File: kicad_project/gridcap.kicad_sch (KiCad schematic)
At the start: 69 parts, among them J1 Conn_01x10

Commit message: Add all pads to pcb
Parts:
- PAD17, PAD18, PAD19, PAD20, PAD21, PAD22, PAD23, PAD24, PAD25, PAD26, PAD27, PAD28, PAD29, PAD30, PAD31, PAD32, PAD33, PAD34, PAD35, PAD36, PAD37, PAD38, PAD39, PAD40, PAD41, PAD42, PAD43, PAD44, PAD45, PAD46, PAD47, PAD48, PAD49, PAD50, PAD51, PAD52, PAD53, PAD54, PAD55, PAD56, PAD57, PAD58, PAD59, PAD60, PAD61, PAD62, PAD63, PAD64: footprint (none) -> gridcap_footprints:CAPACITOR_PAD

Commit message: Fix pad pin number
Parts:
- MUX1, MUX2, MUX3, MUX4, PAD1, PAD10, PAD11, PAD12, PAD13, PAD14, PAD15, PAD16, PAD17, PAD18, PAD19, PAD2, PAD20, PAD21, PAD22, PAD23, PAD24, PAD25, PAD26, PAD27, PAD28, PAD29, PAD3, PAD30, PAD31, PAD32, PAD33, PAD34, PAD35, PAD36, PAD37, PAD38, PAD39, PAD4, PAD40, PAD41, PAD42, PAD43, PAD44, PAD45, PAD46, PAD47, PAD48, PAD49, PAD5, PAD50, PAD51, PAD52, PAD53, PAD54, PAD55, PAD56, PAD57, PAD58, PAD59, PAD6, PAD60, PAD61, PAD62, PAD63, PAD64, PAD7, PAD8, PAD9: value ~ -> (none)
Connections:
- net at MUX2.6 (Y3): now also PAD25.1; no longer PAD25.
- net at MUX2.20 (Y11): now also PAD24.1; no longer PAD24.
- net at MUX4.7 (Y2): now also PAD59.1; no longer PAD59.
- net at MUX3.22 (Y9): now also PAD36.1; no longer PAD36.
- net at MUX4.17 (Y14): now also PAD62.1; no longer PAD62.
- net at MUX2.9 (Y0): now also PAD31.1; no longer PAD31.
- net at MUX2.4 (Y5): now also PAD21.1; no longer PAD21.
- net at MUX1.8 (Y1): now also PAD7.1; no longer PAD7.
- net at MUX2.16 (Y15): now also PAD32.1; no longer PAD32.
- net at MUX4.5 (Y4): now also PAD55.1; no longer PAD55.
- net at MUX2.22 (Y9): now also PAD20.1; no longer PAD20.
- net at MUX3.4 (Y5): now also PAD37.1; no longer PAD37.
- net at MUX2.8 (Y1): now also PAD29.1; no longer PAD29.
- net at MUX3.5 (Y4): now also PAD39.1; no longer PAD39.
- net at MUX1.6 (Y3): now also PAD5.1; no longer PAD5.
- net at MUX1.19 (Y12): now also PAD13.1; no longer PAD13.
- net at MUX2.19 (Y12): now also PAD26.1; no longer PAD26.
- net at MUX3.3 (Y6): now also PAD35.1; no longer PAD35.
- net at MUX4.9 (Y0): now also PAD63.1; no longer PAD63.
- net at MUX3.8 (Y1): now also PAD45.1; no longer PAD45.
- net at MUX4.8 (Y1): now also PAD61.1; no longer PAD61.
- net at MUX4.23 (Y8): now also PAD50.1; no longer PAD50.
- net at MUX2.7 (Y2): now also PAD27.1; no longer PAD27.
- net at MUX2.5 (Y4): now also PAD23.1; no longer PAD23.
- net at MUX2.17 (Y14): now also PAD30.1; no longer PAD30.
- net at MUX3.7 (Y2): now also PAD43.1; no longer PAD43.
- net at MUX2.18 (Y13): now also PAD28.1; no longer PAD28.
- net at MUX2.2 (Y7): now also PAD17.1; no longer PAD17.
- net at MUX2.21 (Y10): now also PAD22.1; no longer PAD22.
- net at MUX2.23 (Y8): now also PAD18.1; no longer PAD18.
- net at MUX2.3 (Y6): now also PAD19.1; no longer PAD19.
- net at MUX1.16 (Y15): now also PAD16.1; no longer PAD16.
- net at MUX1.17 (Y14): now also PAD15.1; no longer PAD15.
- net at MUX1.18 (Y13): now also PAD14.1; no longer PAD14.
- net at MUX1.2 (Y7): now also PAD1.1; no longer PAD1.
- net at MUX1.20 (Y11): now also PAD12.1; no longer PAD12.
- net at MUX1.21 (Y10): now also PAD11.1; no longer PAD11.
- net at MUX1.22 (Y9): now also PAD10.1; no longer PAD10.
- net at MUX1.23 (Y8): now also PAD9.1; no longer PAD9.
- net at MUX1.3 (Y6): now also PAD2.1; no longer PAD2.
- net at MUX1.4 (Y5): now also PAD3.1; no longer PAD3.
- net at MUX1.5 (Y4): now also PAD4.1; no longer PAD4.
- net at MUX1.7 (Y2): now also PAD6.1; no longer PAD6.
- net at MUX1.9 (Y0): now also PAD8.1; no longer PAD8.
- net at MUX3.18 (Y13): now also PAD44.1; no longer PAD44.
- net at MUX4.16 (Y15): now also PAD64.1; no longer PAD64.
- net at MUX4.18 (Y13): now also PAD60.1; no longer PAD60.
- net at MUX4.19 (Y12): now also PAD58.1; no longer PAD58.
- net at MUX4.2 (Y7): now also PAD49.1; no longer PAD49.
- net at MUX4.20 (Y11): now also PAD56.1; no longer PAD56.
- net at MUX4.21 (Y10): now also PAD54.1; no longer PAD54.
- net at MUX4.22 (Y9): now also PAD52.1; no longer PAD52.
- net at MUX4.3 (Y6): now also PAD51.1; no longer PAD51.
- net at MUX4.4 (Y5): now also PAD53.1; no longer PAD53.
- net at MUX4.6 (Y3): now also PAD57.1; no longer PAD57.
- net at MUX3.16 (Y15): now also PAD48.1; no longer PAD48.
- net at MUX3.17 (Y14): now also PAD46.1; no longer PAD46.
- net at MUX3.19 (Y12): now also PAD42.1; no longer PAD42.
- net at MUX3.2 (Y7): now also PAD33.1; no longer PAD33.
- net at MUX3.20 (Y11): now also PAD40.1; no longer PAD40.
- net at MUX3.21 (Y10): now also PAD38.1; no longer PAD38.
- net at MUX3.23 (Y8): now also PAD34.1; no longer PAD34.
- net at MUX3.6 (Y3): now also PAD41.1; no longer PAD41.
- net at MUX3.9 (Y0): now also PAD47.1; no longer PAD47.

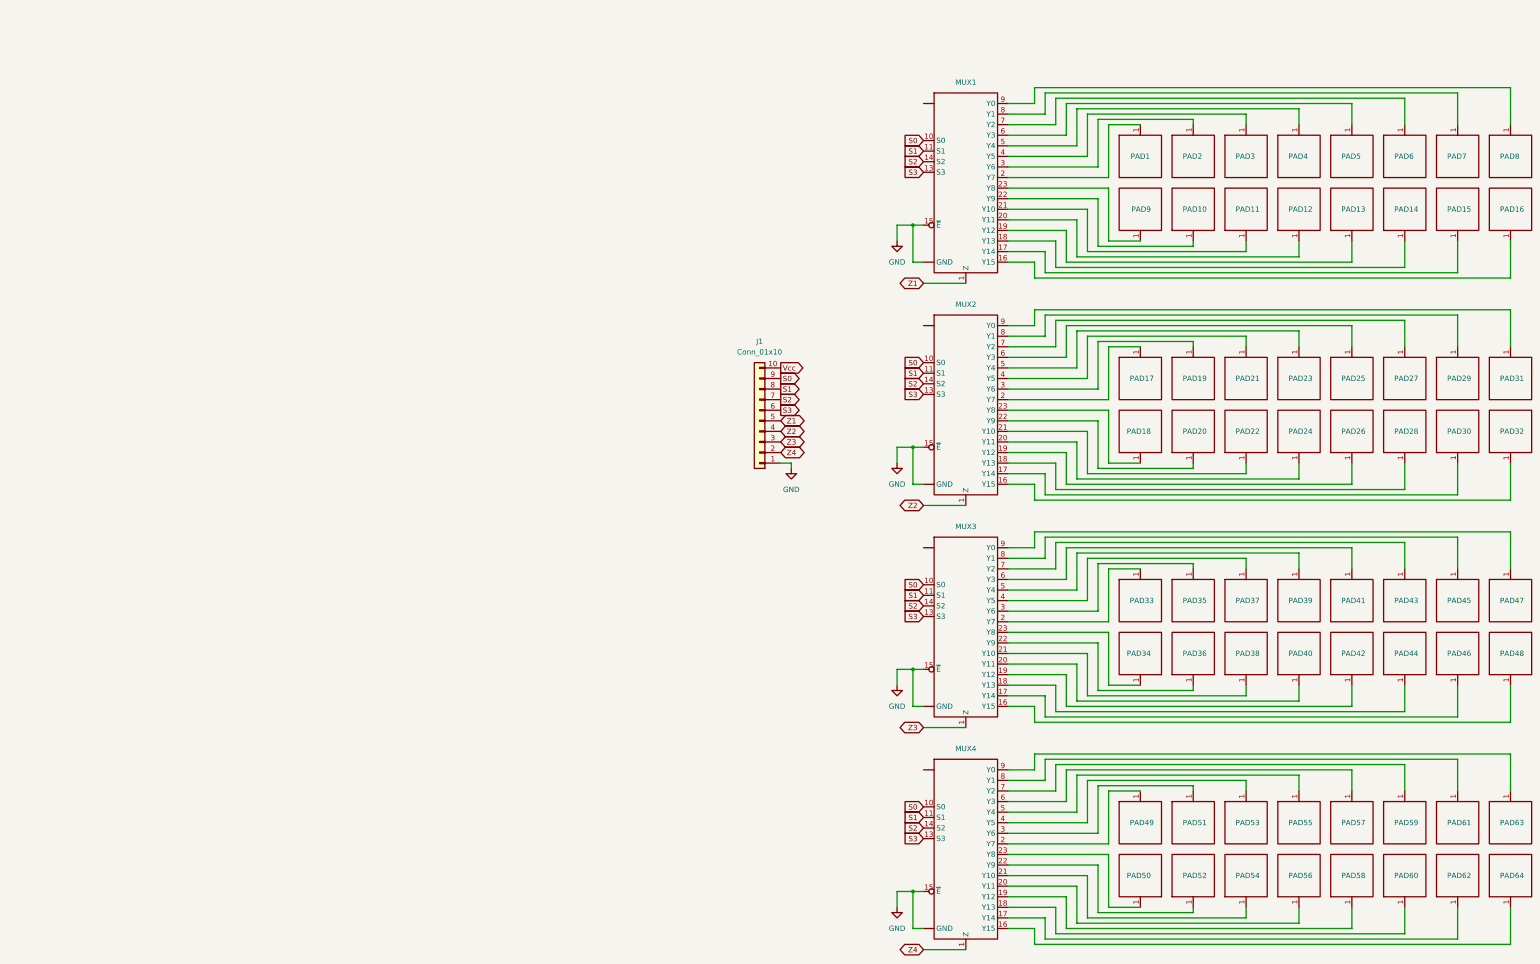
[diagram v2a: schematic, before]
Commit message: Begin rewiring pads and muxes
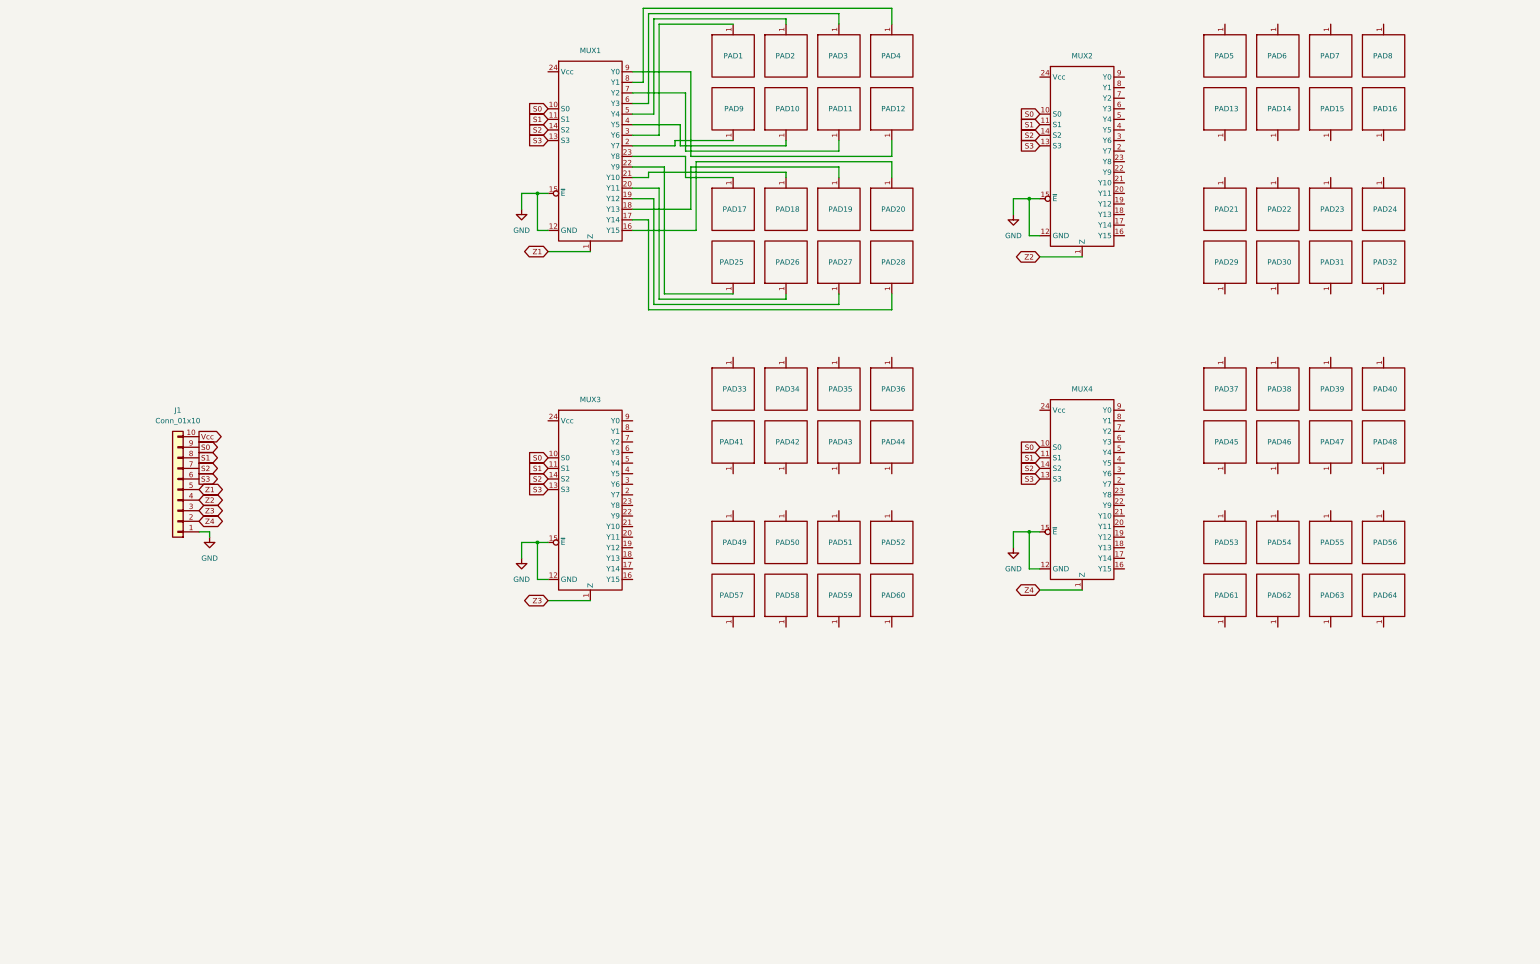
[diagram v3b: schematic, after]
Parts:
- MUX1, MUX2, MUX3, MUX4, PAD1, PAD10, PAD11, PAD12, PAD13, PAD14, PAD15, PAD16, PAD17, PAD18, PAD19, PAD2, PAD20, PAD21, PAD22, PAD23, PAD24, PAD25, PAD26, PAD27, PAD28, PAD29, PAD3, PAD30, PAD31, PAD32, PAD33, PAD34, PAD35, PAD36, PAD37, PAD38, PAD39, PAD4, PAD40, PAD41, PAD42, PAD43, PAD44, PAD45, PAD46, PAD47, PAD48, PAD49, PAD5, PAD50, PAD51, PAD52, PAD53, PAD54, PAD55, PAD56, PAD57, PAD58, PAD59, PAD6, PAD60, PAD61, PAD62, PAD63, PAD64, PAD7, PAD8, PAD9: value (none) -> ~
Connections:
- net GND: now also MUX1.12 (GND), MUX2.12 (GND), MUX3.12 (GND), MUX4.12 (GND); no longer MUX1. (GND), MUX2. (GND), MUX3. (GND), MUX4. (GND)
- net at PAD25.1: now also MUX1.22 (Y9); no longer MUX2.6 (Y3)
- net at PAD24.1: no longer MUX2.20 (Y11)
- net at PAD59.1: no longer MUX4.7 (Y2)
- net at PAD36.1: no longer MUX3.22 (Y9)
- net at PAD62.1: no longer MUX4.17 (Y14)
- net at PAD31.1: no longer MUX2.9 (Y0)
- net at PAD21.1: no longer MUX2.4 (Y5)
- net at PAD7.1: no longer MUX1.8 (Y1)
- net at PAD32.1: no longer MUX2.16 (Y15)
- net at PAD55.1: no longer MUX4.5 (Y4)
- net at PAD20.1: now also MUX1.16 (Y15); no longer MUX2.22 (Y9)
- net at PAD37.1: no longer MUX3.4 (Y5)
- net at PAD29.1: no longer MUX2.8 (Y1)
- net at PAD39.1: no longer MUX3.5 (Y4)
- net at PAD5.1: no longer MUX1.6 (Y3)
- net at PAD13.1: no longer MUX1.19 (Y12)
- net at PAD26.1: now also MUX1.20 (Y11); no longer MUX2.19 (Y12)
- net at PAD35.1: no longer MUX3.3 (Y6)
- net at PAD63.1: no longer MUX4.9 (Y0)
- net at PAD45.1: no longer MUX3.8 (Y1)
- net at PAD61.1: no longer MUX4.8 (Y1)
- net at PAD50.1: no longer MUX4.23 (Y8)
- net at PAD27.1: now also MUX1.19 (Y12); no longer MUX2.7 (Y2)
- net at PAD23.1: no longer MUX2.5 (Y4)
- net at PAD30.1: no longer MUX2.17 (Y14)
- net at PAD43.1: no longer MUX3.7 (Y2)
- net at MUX2.18 (Y13): no longer PAD28.1
- net at MUX2.2 (Y7): no longer PAD17.1
- net at MUX2.21 (Y10): no longer PAD22.1
- net at MUX2.23 (Y8): no longer PAD18.1
- net at MUX2.3 (Y6): no longer PAD19.1
- net at PAD16.1: no longer MUX1.16 (Y15)
- net at MUX1.17 (Y14): now also PAD28.1; no longer PAD15.1
- net at MUX1.18 (Y13): now also PAD19.1; no longer PAD14.1
- net at MUX1.2 (Y7): now also PAD9.1; no longer PAD1.1
- net at PAD12.1: now also MUX1.9 (Y0); no longer MUX1.20 (Y11)
- net at MUX1.21 (Y10): now also PAD18.1; no longer PAD11.1
- net at PAD10.1: now also MUX1.4 (Y5); no longer MUX1.22 (Y9)
- net at MUX1.23 (Y8): now also PAD17.1; no longer PAD9.1
- net at MUX1.3 (Y6): now also PAD1.1; no longer PAD2.1
- net at PAD3.1: now also MUX1.6 (Y3); no longer MUX1.4 (Y5)
- net at MUX1.5 (Y4): now also PAD2.1; no longer PAD4.1
- net at MUX1.7 (Y2): now also PAD11.1; no longer PAD6.1
- net at PAD8.1: no longer MUX1.9 (Y0)
- net at PAD44.1: no longer MUX3.18 (Y13)
- net at MUX4.16 (Y15): no longer PAD64.1
- net at MUX4.18 (Y13): no longer PAD60.1
- net at MUX4.19 (Y12): no longer PAD58.1
- net at MUX4.2 (Y7): no longer PAD49.1
- net at MUX4.20 (Y11): no longer PAD56.1
- net at MUX4.21 (Y10): no longer PAD54.1
- net at MUX4.22 (Y9): no longer PAD52.1
- net at MUX4.3 (Y6): no longer PAD51.1
- net at MUX4.4 (Y5): no longer PAD53.1
- net at MUX4.6 (Y3): no longer PAD57.1
- net at MUX3.16 (Y15): no longer PAD48.1
- net at MUX3.17 (Y14): no longer PAD46.1
- net at MUX3.19 (Y12): no longer PAD42.1
- net at MUX3.2 (Y7): no longer PAD33.1
- net at MUX3.20 (Y11): no longer PAD40.1
- net at MUX3.21 (Y10): no longer PAD38.1
- net at MUX3.23 (Y8): no longer PAD34.1
- net at MUX3.6 (Y3): no longer PAD41.1
- net at MUX3.9 (Y0): no longer PAD47.1
- new net: MUX1.8 (Y1), PAD4.1
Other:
- moved on the sheet: J1, PAD1, PAD10, PAD11, PAD12, PAD13, PAD14, PAD15, PAD16, PAD17, PAD18, PAD19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

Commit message: Route all muxes to pads
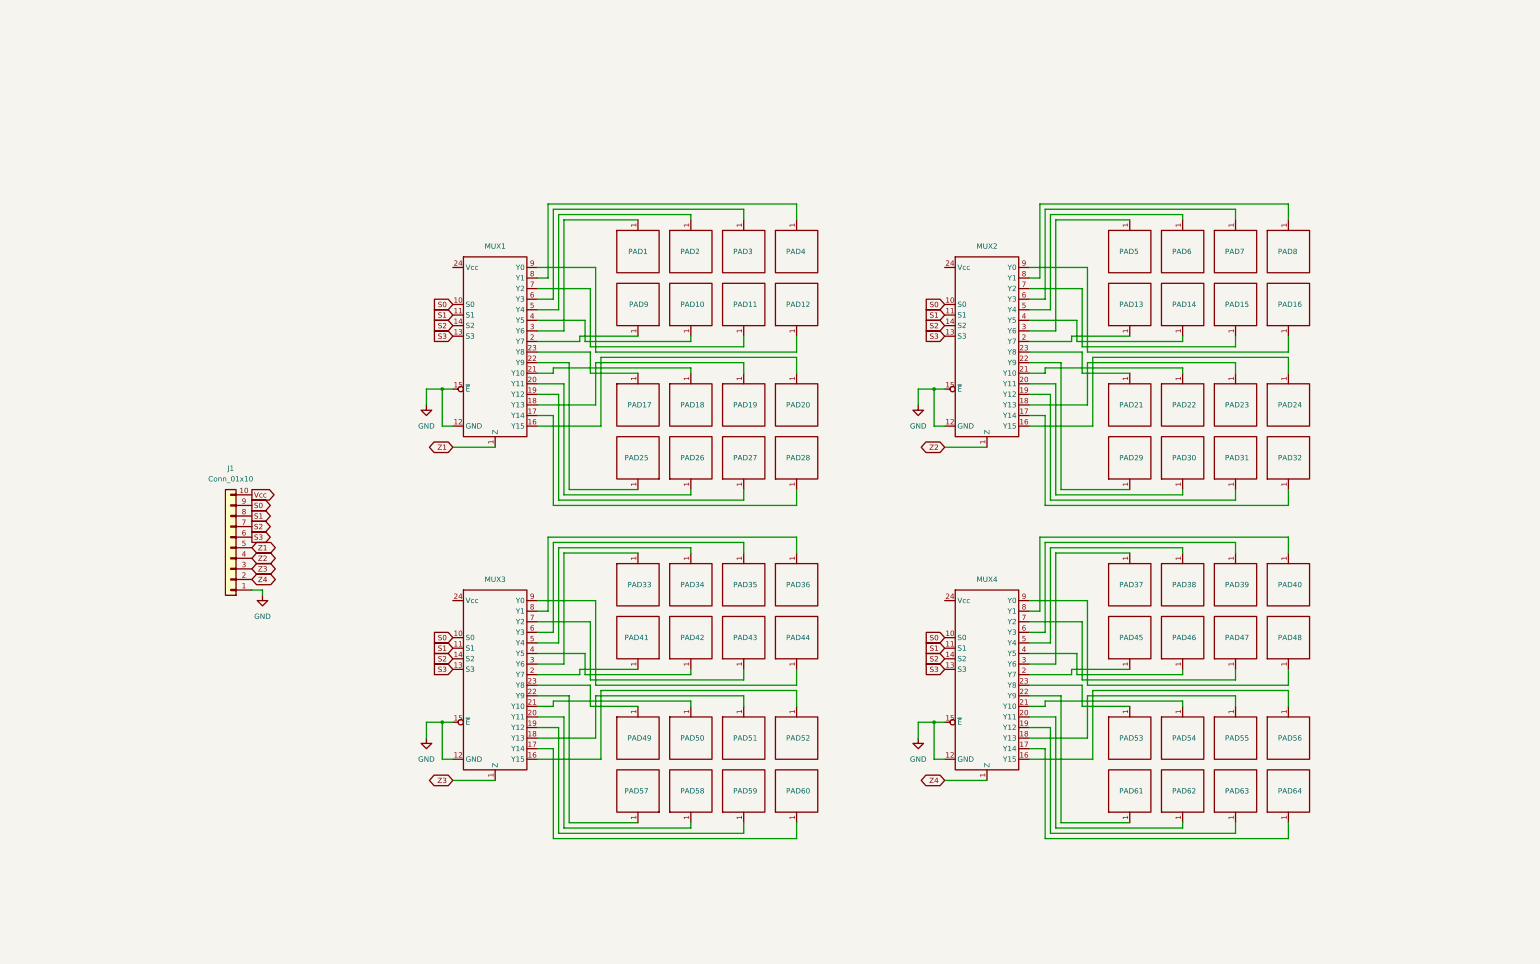
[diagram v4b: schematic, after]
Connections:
- net at PAD24.1: now also MUX2.16 (Y15)
- net at PAD59.1: now also MUX3.19 (Y12)
- net at PAD36.1: now also MUX3.8 (Y1)
- net at PAD62.1: now also MUX4.20 (Y11)
- net at PAD31.1: now also MUX2.19 (Y12)
- net at PAD21.1: now also MUX2.23 (Y8)
- net at PAD7.1: now also MUX2.6 (Y3)
- net at PAD32.1: now also MUX2.17 (Y14)
- net at PAD55.1: now also MUX4.18 (Y13)
- net at PAD37.1: now also MUX4.3 (Y6)
- net at PAD29.1: now also MUX2.22 (Y9)
- net at PAD39.1: now also MUX4.6 (Y3)
- net at PAD5.1: now also MUX2.3 (Y6)
- net at PAD13.1: now also MUX2.2 (Y7)
- net at PAD35.1: now also MUX3.6 (Y3)
- net at PAD63.1: now also MUX4.19 (Y12)
- net at PAD45.1: now also MUX4.2 (Y7)
- net at PAD61.1: now also MUX4.22 (Y9)
- net at PAD50.1: now also MUX3.21 (Y10)
- net at PAD23.1: now also MUX2.18 (Y13)
- net at PAD30.1: now also MUX2.20 (Y11)
- net at PAD43.1: now also MUX3.7 (Y2)
- net at MUX2.21 (Y10): now also PAD22.1
- net at MUX2.4 (Y5): now also PAD14.1
- net at MUX2.5 (Y4): now also PAD6.1
- net at MUX2.7 (Y2): now also PAD15.1
- net at MUX2.8 (Y1): now also PAD8.1
- net at MUX2.9 (Y0): now also PAD16.1
- net at PAD44.1: now also MUX3.9 (Y0)
- net at MUX4.16 (Y15): now also PAD56.1
- net at MUX4.17 (Y14): now also PAD64.1
- net at MUX4.21 (Y10): now also PAD54.1
- net at MUX4.23 (Y8): now also PAD53.1
- net at MUX4.4 (Y5): now also PAD46.1
- net at MUX4.5 (Y4): now also PAD38.1
- net at MUX4.7 (Y2): now also PAD47.1
- net at MUX4.8 (Y1): now also PAD40.1
- net at MUX4.9 (Y0): now also PAD48.1
- net at PAD60.1: now also MUX3.17 (Y14)
- net at MUX3.16 (Y15): now also PAD52.1
- net at MUX3.18 (Y13): now also PAD51.1
- net at MUX3.2 (Y7): now also PAD41.1
- net at MUX3.20 (Y11): now also PAD58.1
- net at MUX3.22 (Y9): now also PAD57.1
- net at MUX3.23 (Y8): now also PAD49.1
- net at MUX3.3 (Y6): now also PAD33.1
- net at MUX3.4 (Y5): now also PAD42.1
- net at MUX3.5 (Y4): now also PAD34.1
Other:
- moved on the sheet: J1, MUX1, MUX2, MUX3, MUX4, PAD1, PAD10, PAD11, PAD12, PAD13, PAD14, PAD15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

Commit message: Route all muxes and add pcb shape
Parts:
- J1: footprint (none) -> Connector_PinHeader_2.54mm:PinHeader_1x10_P2.54mm_Vertical
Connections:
- net Vcc: now also MUX1.24 (Vcc), MUX2.24 (Vcc), MUX3.24 (Vcc), MUX4.24 (Vcc)
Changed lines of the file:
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@@
+    )
+  )
+  (global_label "Vcc" (shape input) (at 129.54 81.28 180) (fields_autoplaced)
+    (effects (font (size 1.27 1.27)) (justify right))
+    (property "Intersheetrefs" "${INTERSHEET_REFS}" (at 123.289 81.28 0)
+      (effects (font (size 1.27 1.27)) (justify right) hide)
     )
   )
@@
     )
   )
+  (global_label "Vcc" (shape input) (at 247.65 161.29 180) (fields_autoplaced)
+    (effects (font (size 1.27 1.27)) (justify right))
+    (property "Intersheetrefs" "${INTERSHEET_REFS}" (at 241.399 161.29 0)
+      (effects (font (size 1.27 1.27)) (justify right) hide)
+    )
+  )
   (global_label "S2" (shape input) (at 247.65 95.25 180) (fields_autoplaced)
     (effects (font (size 1.27 1.27)) (justify right))
@@
     )
   )
+  (global_label "Vcc" (shape input) (at 129.54 161.29 180) (fields_autoplaced)
+    (effects (font (size 1.27 1.27)) (justify right))
+    (property "Intersheetrefs" "${INTERSHEET_REFS}" (at 123.289 161.29 0)
+      (effects (font (size 1.27 1.27)) (justify right) hide)
+    )
+  )
   (global_label "S2" (shape output) (at 81.28 143.51 0) (fields_autoplaced)
     (effects (font (size 1.27 1.27)) (justify left))
@@
     )
   )
+  (global_label "Vcc" (shape input) (at 247.65 81.28 180) (fields_autoplaced)
+    (effects (font (size 1.27 1.27)) (justify right))
+    (property "Intersheetrefs" "${INTERSHEET_REFS}" (at 241.399 81.28 0)
+      (effects (font (size 1.27 1.27)) (justify right) hide)
+    )
+  )
   (global_label "Z4" (shape bidirectional) (at 247.65 204.47 180) (fields_autoplaced)
     (effects (font (size 1.27 1.27)) (justify right))
@@
       (effects (font (size 1.27 1.27)))
     )
-    (property "Footprint" "" (at 76.2 148.59 0)
-      (effects (font (size 1.27 1.27)) hide)
-    )
+    (property "Footprint" "Connector_PinHeader_2.54mm:PinHeader_1x10_P2.54mm_Vertical" (at 76.2 148.59 0)
+      (effects (font (size 1.27 1.27)) hide)
+    )

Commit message: add reader schematic
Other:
- added sheet Reader (reader.kicad_sch)
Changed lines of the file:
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@@
+    )
+  )
+  (sheet (at 22.86 22.86) (size 82.55 53.34) (fields_autoplaced)
+    (stroke (width 0.1524) (type solid))
+    (fill (color 0 0 0 0.0000))
+    (property "Sheetname" "Reader" (at 22.86 22.1484 0)
+      (effects (font (size 1.27 1.27)) (justify left bottom))
+    )
+    (property "Sheetfile" "reader.kicad_sch" (at 22.86 76.7846 0)
+      (effects (font (size 1.27 1.27)) (justify left top))
+    )
+    (instances
+      (project "gridcap"
+        (path "/78a49c71-2951-48b9-8f1e-813ada77e8b7" (page "2"))
+      )
     )
   )
